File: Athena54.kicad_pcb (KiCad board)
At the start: 4 copper layers, 137.4 x 107 mm, 106 parts, among them J1 BATT, J2 HRO_TYPE-C-31-M-12, J3 JTAG_TC2030, J4 RGB, Q1 2N7002, Q2 2N7002, Q3 AO3407, SW1 POWER, SW10 MX Hotswap, SW11 MX Hotswap, SW12 MX Hotswap, SW13 MX Hotswap, SW14 MX Hotswap, SW15 MX Hotswap, SW16 MX Hotswap, SW17 MX Hotswap, SW18 MX Hotswap, SW19 MX Hotswap, SW2 MX Hotswap, SW20 MX Hotswap, SW21 MX Hotswap, SW22 MX Hotswap, SW23 MX Hotswap, SW24 MX Hotswap, SW25 MX Hotswap, SW26 MX Hotswap, SW27 MX Hotswap, SW28 MX Hotswap, SW29 RESET, SW3 MX Hotswap, SW4 MX Hotswap, SW5 MX Hotswap, SW6 MX Hotswap, SW7 MX Hotswap, SW8 MX Hotswap, SW9 MX Hotswap, U1 BQ24075RGT, U2 MAX17048, U3 USBLC6-2SC6, U4 nRF52840_moko_mk08

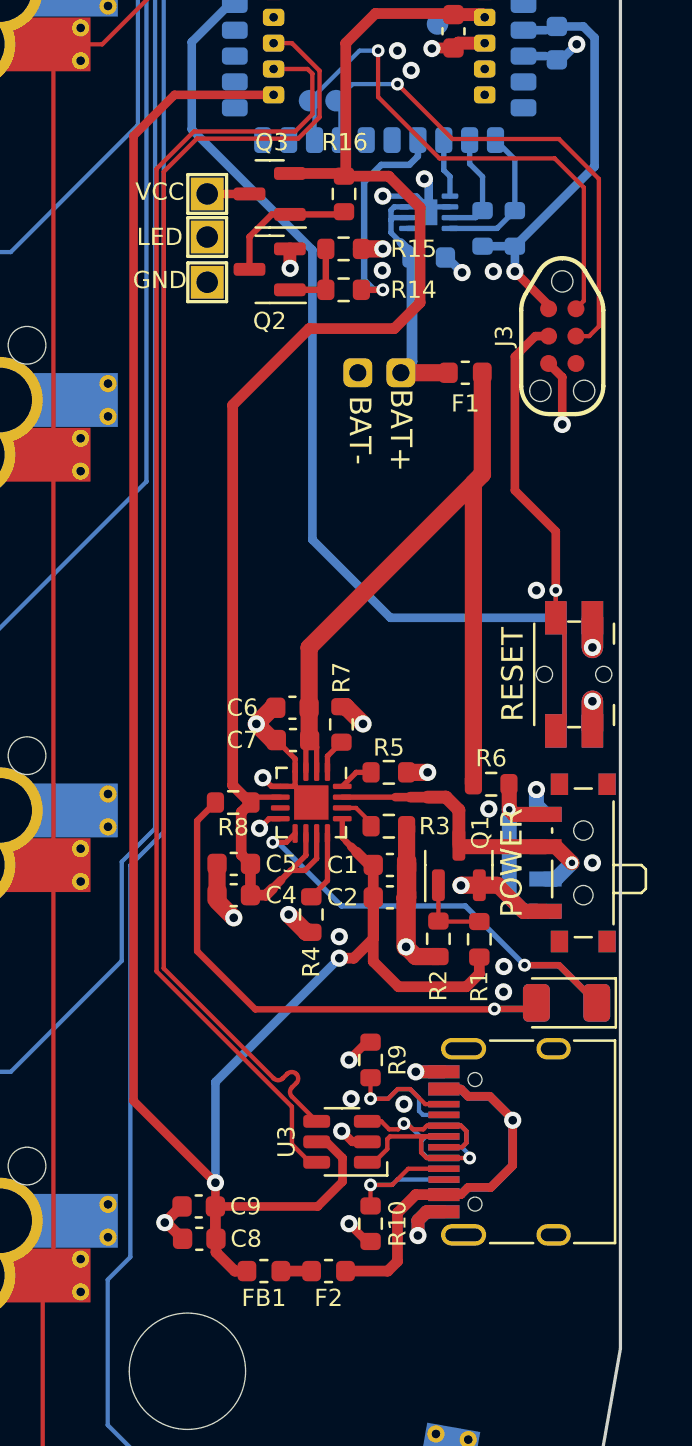
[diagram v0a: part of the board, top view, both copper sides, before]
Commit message: fix(pcb): Move USB-C 1.5mm closer to the edge
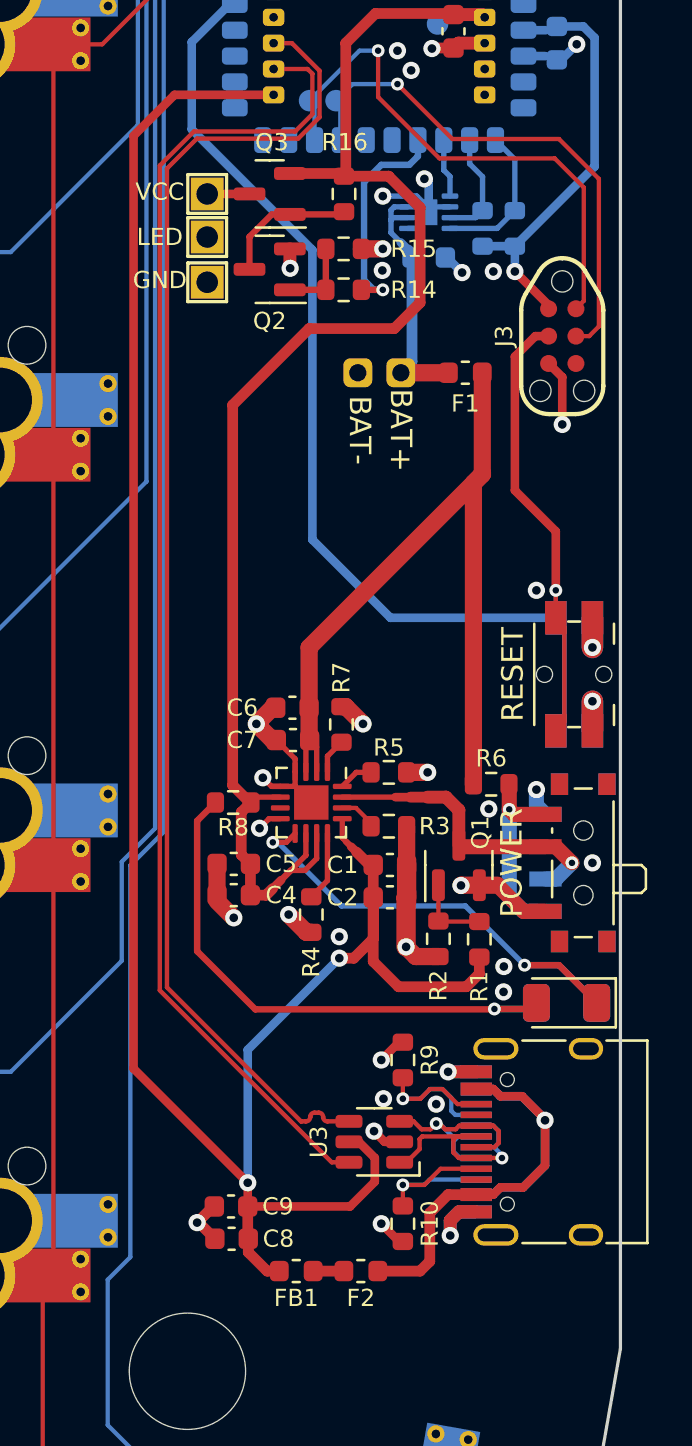
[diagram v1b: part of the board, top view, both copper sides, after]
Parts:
- moved C8 1.50 mm to (109.8, 59.5)
- moved C9 1.50 mm to (109.8, 58.0)
- moved F2 1.50 mm to (115.8, 61.0)
- moved FB1 1.50 mm to (112.8, 61.0)
- moved J2 1.50 mm to (125.2, 55.0)
- moved R10 1.50 mm to (117.8, 58.8)
- moved R9 1.50 mm to (117.8, 51.2)
- moved U3 1.50 mm to (116.5, 55.0)
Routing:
- net DO-: track 61.1 -> 62.2 mm
- net DO+: track 61.3 -> 62.4 mm

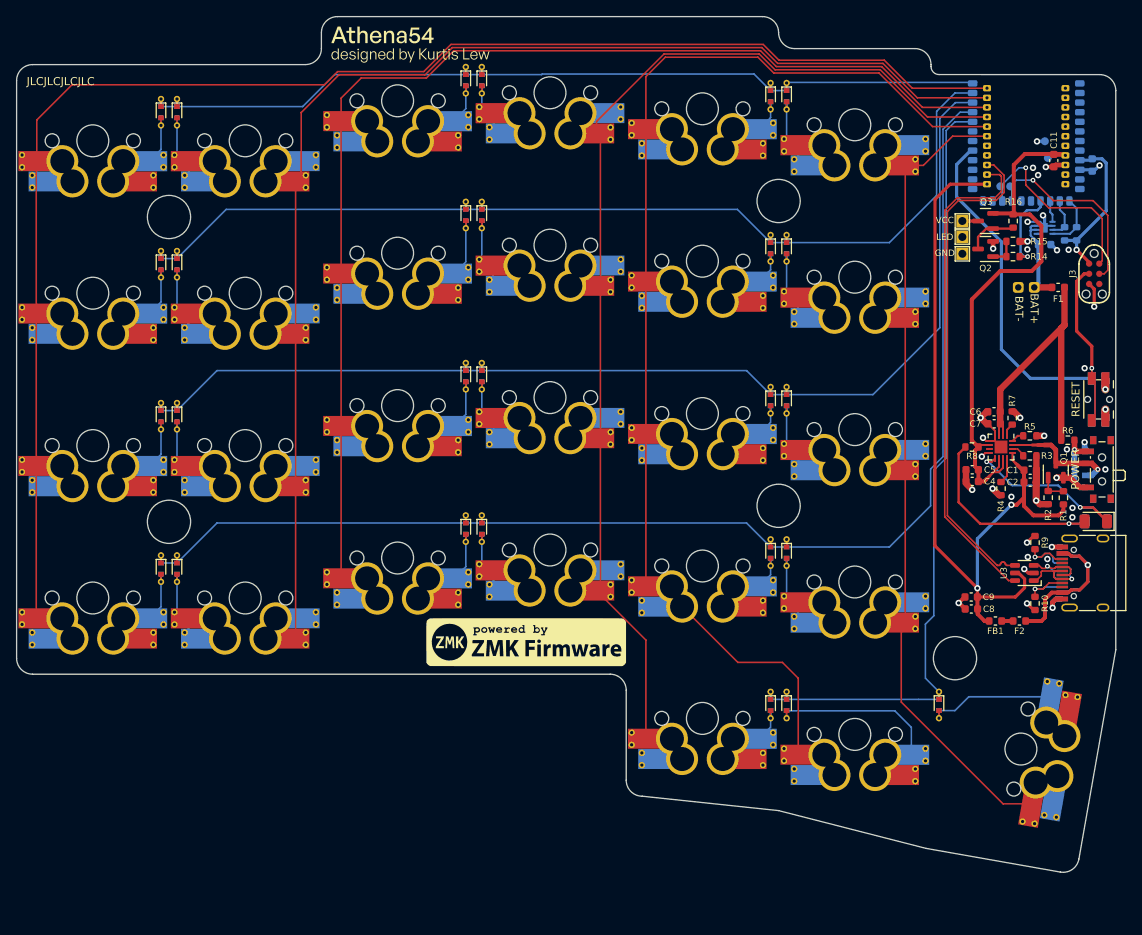
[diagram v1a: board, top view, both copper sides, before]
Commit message: fix(pcb): Move thumb cluster in by 3mm
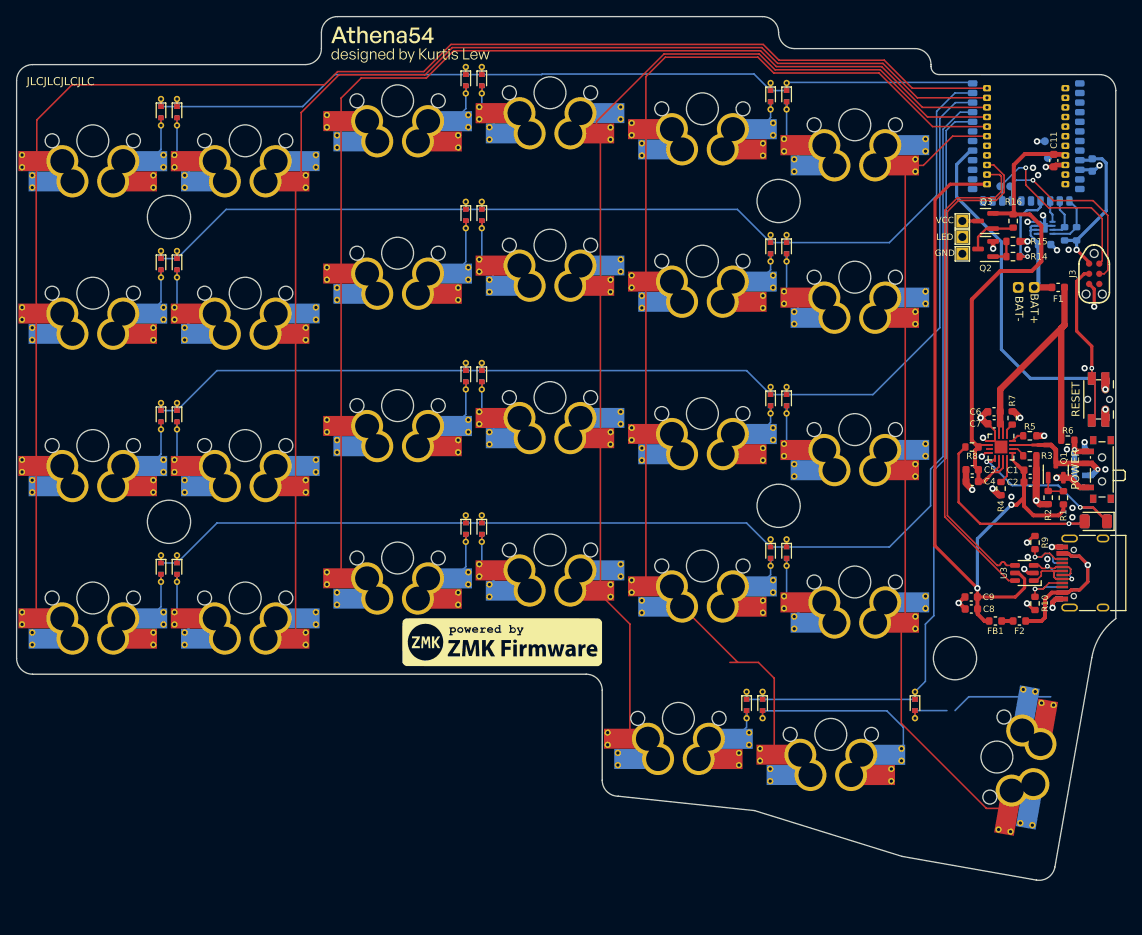
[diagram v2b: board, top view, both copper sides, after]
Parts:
- moved SW28 3.16 mm to (113.0, 78.0)
- moved D19 3.00 mm to (81.7, 71.5)
- moved D24 3.00 mm to (83.7, 71.5)
- moved D29 3.00 mm to (102.8, 71.5)
- moved G1 3.00 mm to (51.2, 63.7) (x2)
- moved SW18 3.00 mm to (73.2, 73.2)
- moved SW23 3.00 mm to (92.2, 75.2)
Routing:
- net Net-(D24-Pad2): track 21.7 -> 23.8 mm
- net COL5: track 138.7 -> 136.7 mm
- net Net-(D29-Pad2): track 16.6 -> 18.6 mm
- net COL6: track 97.6 -> 96.6 mm
- net COL4: track 132.3 -> 131.5 mm
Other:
- board size 137.4 x 107 mm -> 137.4 x 108 mm

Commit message: feat(pcb): Version 0.2
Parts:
- removed C12: 100nF, Capacitor_SMD:C_0603_1608Metric
- removed G*** (x2): LOGO, Conejo:Athena54
- removed R15, R16: 10K, Resistor_SMD:R_0603_1608Metric
- removed the R8 at (109.9, 39.3)
- added C10: 4.7uF, Capacitor_SMD:C_0402_1005Metric, B.Cu at (109.4, 5.45)
- added L1: NC, Inductor_SMD:L_0402_1005Metric, B.Cu at (108.9, 4.05)
- added R10: 100R, Resistor_SMD:R_0402_1005Metric, B.Cu at (107.5, 50.1)
- added R11: 1K5, Resistor_SMD:R_0402_1005Metric, F.Cu at (114.0, 0.90)
- C1, C2, C4, C5, C6, C7, C8, C9: footprint Capacitor_SMD:C_0603_1608Metric -> Capacitor_SMD:C_0402_1005Metric; moved to B.Cu
- C11, C3: footprint Capacitor_SMD:C_0603_1608Metric -> Capacitor_SMD:C_0402_1005Metric
- F1, J1, J4, Q1, Q2, Q3, U1: moved to B.Cu
- F2: footprint Fuse:Fuse_0603_1608Metric -> Fuse:Fuse_0402_1005Metric; moved to B.Cu
- FB1: footprint Inductor_SMD:L_0603_1608Metric -> Inductor_SMD:L_0402_1005Metric; moved to B.Cu
- G1: moved to F.Cu
- G2: renamed from G1; moved to B.Cu
- H1, H2, H3, H4, H5: footprint Athena54:MountingHole_5.4mm -> Athena54:MountingHole_4.3mm
- J2: footprint Conejo:USB_C_Receptacle_HRO_TYPE-C-31-M-12 (Reversible) -> Athena54:USB_C_Receptacle_HRO_TYPE-C-31-M-12 (Reversible)
- R1, R2, R3: footprint Resistor_SMD:R_0603_1608Metric -> Resistor_SMD:R_0402_1005Metric; moved to B.Cu
- R12: footprint Resistor_SMD:R_0603_1608Metric -> Resistor_SMD:R_0402_1005Metric; moved to F.Cu
- R13: value 1K5 -> 10K; footprint Resistor_SMD:R_0603_1608Metric -> Resistor_SMD:R_0402_1005Metric
- R14: value 100 -> 10K; footprint Resistor_SMD:R_0603_1608Metric -> Resistor_SMD:R_0402_1005Metric; moved to B.Cu
- R4: value RLIM -> RSET; footprint Resistor_SMD:R_0603_1608Metric -> Resistor_SMD:R_0402_1005Metric; moved to B.Cu
- R5: value RSET -> 100K; footprint Resistor_SMD:R_0603_1608Metric -> Resistor_SMD:R_0402_1005Metric; moved to B.Cu
- R6: value 100K -> 10K; footprint Resistor_SMD:R_0603_1608Metric -> Resistor_SMD:R_0402_1005Metric; moved to B.Cu
- R7: value 10K -> 1K5; footprint Resistor_SMD:R_0603_1608Metric -> Resistor_SMD:R_0402_1005Metric; moved to B.Cu
- R8: renamed from R9; footprint Resistor_SMD:R_0603_1608Metric -> Resistor_SMD:R_0402_1005Metric; moved to B.Cu
- R9: renamed from R10; footprint Resistor_SMD:R_0603_1608Metric -> Resistor_SMD:R_0402_1005Metric; moved to B.Cu
- SW10, SW11, SW12, SW13, SW18, SW19, SW2, SW20, SW21, SW22, SW23, SW3, SW4, SW5: footprint Athena54:MXOnly-1U-Hotswap-Antishear (reversible) -> Athena54:MXOnly-1U-Hotswap (Reversible); moved to F.Cu
- SW14, SW15, SW16, SW17, SW24, SW25, SW26, SW27, SW6, SW7, SW8, SW9: footprint Athena54:MXOnly-1U-Hotswap-Antishear (reversible) -> Athena54:MXOnly-1U-Hotswap (Reversible)
- SW28: footprint Athena54:MXOnly-1.5U-Hotswap-Antishear (reversible) -> Athena54:MXOnly-1.5U-Hotswap (Reversible)
- U3: value USBLC6-2SC6 -> SRV05-4; moved to B.Cu
- U4: value nRF52840_moko_mk08 -> MS88SF3; footprint marbastlib-various:nRF52840_moko_mk08 -> Athena54:MS88SF3
- moved F2 44.3 mm to (112.4, 16.8), turned to -90 degrees
- moved J2 43.1 mm to (118.2, 12.5)
- moved R9 42.5 mm to (111.4, 16.8)
- moved U3 42.5 mm to (110.5, 13.0), turned to -90 degrees
- moved FB1 42.2 mm to (112.4, 18.9), turned to -90 degrees
- moved R8 41.9 mm to (111.4, 9.85)
- moved C8 40.7 mm to (111.4, 18.9), turned to -90 degrees
- moved C9 39.2 mm to (110.4, 18.9), turned to -90 degrees
- moved R13 38.2 mm to (107.5, 48.1)
- moved J4 34.4 mm to (112.8, 47.1), turned to 180 degrees
- moved Q3 34.2 mm to (109.9, 45.1), turned to 0 degrees
- moved Q2 34.1 mm to (109.9, 48.6), turned to 0 degrees
- moved D1 30.7 mm to (118.2, 18.7)
- moved R14 30.6 mm to (107.4, 45.1), turned to 90 degrees
- moved J3 28.2 mm to (114.3, -8.43), turned to 0 degrees
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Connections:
- D1 pad 1: /Power Management/CHG -> Net-(D1-Pad1)
- D1 pad 2: Net-(D1-Pad2) -> VDDH
- J2 pad A6: DI+ -> D+
- J2 pad A7: DI- -> D-
- J2 pad B6: DI+ -> D+
- J2 pad B7: DI- -> D-
- J4 pad 2: LED -> LED_MOSI
- R12 pad 1: SDA -> SCL
- R13 pad 1: SCL -> GND
- R13 pad 2: VDD -> Net-(Q2-Pad1)
- R14 pad 1: EXT_PWR_EN -> Net-(Q2-Pad3)
- R14 pad 2: Net-(Q2-Pad1) -> VDDH
- R4 pad 2: /Power Management/ILIM -> /Power Management/ISET
- R5 pad 1: GND -> Net-(R5-Pad1)
- R5 pad 2: /Power Management/ISET -> VBAT
- R6 pad 1: Net-(R6-Pad1) -> GND
- R6 pad 2: VBAT -> /Power Management/TS
- R7 pad 1: GND -> /Power Management/CHG
- R7 pad 2: /Power Management/TS -> Net-(D1-Pad1)
- SW1 pad 3: Net-(R6-Pad1) -> Net-(R5-Pad1)
- U1 pad 12: /Power Management/ILIM -> unconnected-(U1-Pad12)
- U3 pad 1: DI- -> unconnected-(U3-Pad1)
- U3 pad 3: DI+ -> D-
- U3 pad 4: DO+ -> D+
- U3 pad 6: DO- -> unconnected-(U3-Pad6)
- U4 pad 1: unconnected-(U4-Pad1) -> GND
- U4 pad 10: GND -> unconnected-(U4-Pad10)
- U4 pad 13: SDA -> unconnected-(U4-Pad13)
- U4 pad 14: SCL -> unconnected-(U4-Pad14)
- U4 pad 15: ALERT -> unconnected-(U4-Pad15)
- U4 pad 16: EXT_PWR_EN -> unconnected-(U4-Pad16)
- U4 pad 18: unconnected-(U4-Pad18) -> GND
- U4 pad 19: SWDCLK -> unconnected-(U4-Pad19)
- U4 pad 20: SWDIO -> unconnected-(U4-Pad20)
- U4 pad 25: unconnected-(U4-Pad25) -> SDA
- U4 pad 26: unconnected-(U4-Pad26) -> SCL
- U4 pad 27: RESET -> ALERT
- U4 pad 28: unconnected-(U4-Pad28) -> RESET
- U4 pad 30: ROW5 -> unconnected-(U4-Pad30)
- U4 pad 31: ROW4 -> VDD
- U4 pad 32: ROW3 -> VDDH
- U4 pad 33: ROW2 -> DCCH
- U4 pad 34: ROW1 -> GND
- U4 pad 35: unconnected-(U4-Pad35) -> +5V
- U4 pad 36: unconnected-(U4-Pad36) -> D-
- U4 pad 37: unconnected-(U4-Pad37) -> D+
- U4 pad 39: GND -> unconnected-(U4-Pad39)
- U4 pad 40: unconnected-(U4-Pad40) -> EXT_PWR_EN
- U4 pad 41: unconnected-(U4-Pad41) -> LED_MOSI
- U4 pad 42: VDDH -> ROW5
- U4 pad 43: GND -> ROW4
- U4 pad 44: unconnected-(U4-Pad44) -> ROW3
- U4 pad 45: unconnected-(U4-Pad45) -> ROW2
- U4 pad 46: +5V -> COL6
- U4 pad 47: DO- -> ROW1
- U4 pad 48: DO+ -> COL5
- U4 pad 49: unconnected-(U4-Pad49) -> SWDIO
- U4 pad 50: unconnected-(U4-Pad50) -> SWDCLK
- U4 pad 51: COL6 -> unconnected-(U4-Pad51)
- U4 pad 52: COL5 -> unconnected-(U4-Pad52)
- U4 pad 53: COL4 -> unconnected-(U4-Pad53)
- U4 pad 54: COL3 -> unconnected-(U4-Pad54)
- U4 pad 55: COL2 -> unconnected-(U4-Pad55)
- U4 pad 56: COL1 -> unconnected-(U4-Pad56)
- U4 pad 57: GND -> COL1
- U4 pad 9: VDD -> unconnected-(U4-Pad9)
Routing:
- net DO+: track 62.4 -> 0.00 mm
- net DO-: track 62.2 -> 0.00 mm
- net +5V: track 101.7 -> 39.9 mm
- net LED_MOSI: track 0.00 -> 60.0 mm, vias 0 -> 1
- net +BATT: track 12.0 -> 61.4 mm, vias 0 -> 1
- net EXT_PWR_EN: track 10.3 -> 55.1 mm, vias 1 -> 0
- net D+: track 0.00 -> 30.8 mm, vias 0 -> 1
- net VBAT: track 37.8 -> 7.67 mm
- net RESET: track 65.7 -> 94.1 mm, vias 1 -> 2
- net D-: track 0.00 -> 27.3 mm, vias 0 -> 1
- net Net-(D1-Pad2): track 26.3 -> 0.00 mm, vias 1 -> 0
- net COL5: track 136.7 -> 112.2 mm, vias 0 -> 1
- net GND: track 64.2 -> 40.3 mm, vias 39 -> 60
- net /Power Management/CHG: track 23.4 -> 1.57 mm, vias 2 -> 0
- net Net-(D1-Pad1): track 0.00 -> 18.8 mm, vias 0 -> 2
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- added copper zone on B.Cu, net GND
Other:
- board size 137.4 x 108 mm -> 130.3 x 112.7 mm
- board text removed: "POWER"
- board text removed: "RESET"

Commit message: feat(pcb): Version 0.2.1
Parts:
- F2: footprint Fuse:Fuse_0402_1005Metric -> Fuse:Fuse_0603_1608Metric
- SW1: footprint Athena54:SW_SPDT_PCM12 (Reversible) -> Athena54:SW_MSK12C02-HB (Reversible)
- moved R1 0.83 mm to (114.6, 21.5)
- moved C8 0.42 mm to (111.0, 18.9)
- moved R9 0.42 mm to (111.0, 16.8)
- moved C9 0.35 mm to (110.0, 18.9)
- moved F2 0.32 mm to (112.4, 16.5)
- moved SW1 0.23 mm to (119.0, 27.5), turned to -90 degrees
- moved Q1 0.12 mm to (115.6, 23.9)
- moved R2 0.08 mm to (116.6, 21.5)
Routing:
- net +5V: track 39.9 -> 37.9 mm
- net Net-(R5-Pad1): track 9.00 -> 10.2 mm
- net Net-(Q1-Pad1): track 3.50 -> 2.68 mm
- net /USB-C/CC1: track 7.70 -> 8.40 mm
- net VBUS: track 21.8 -> 21.1 mm
- net GND: track 40.3 -> 39.8 mm, vias 60 -> 59
